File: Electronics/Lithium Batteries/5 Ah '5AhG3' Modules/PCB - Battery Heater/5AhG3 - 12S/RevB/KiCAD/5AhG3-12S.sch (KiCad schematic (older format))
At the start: 129 parts, among them J1 Screw_Terminal_01x02, J2 Screw_Terminal_01x02, J3 Screw_Terminal_01x03, J4 Screw_Terminal_01x03, J5 Conn_01x02, Q1 Q_NMOS_GDS, U1 APV1121S

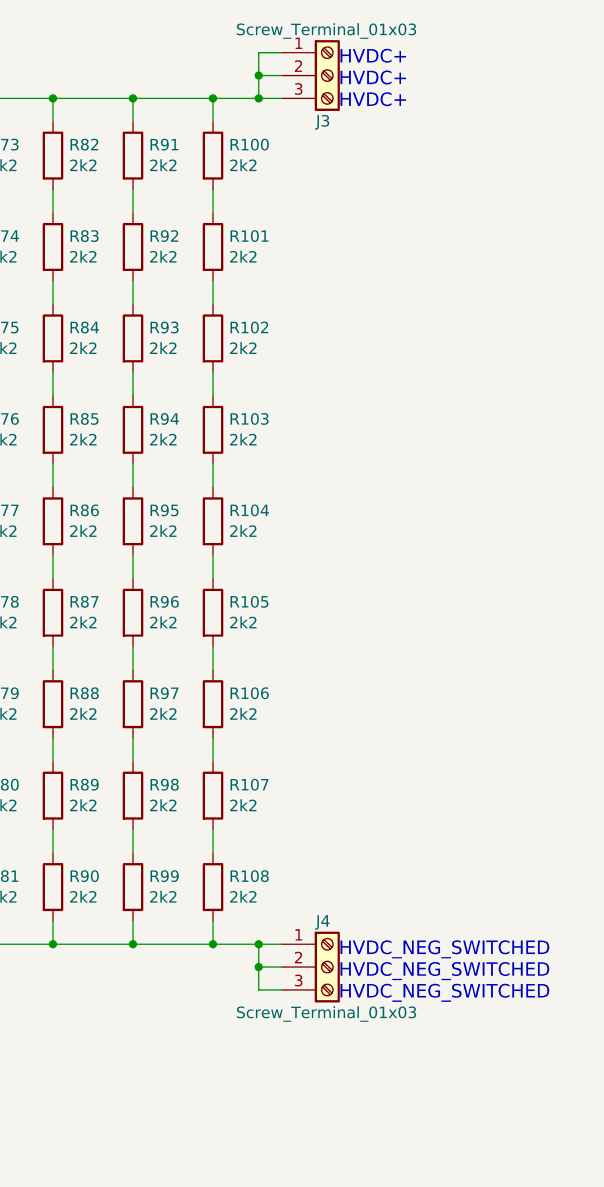
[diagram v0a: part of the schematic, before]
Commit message: RevB Heater PCBs, Daughterboard Schematic
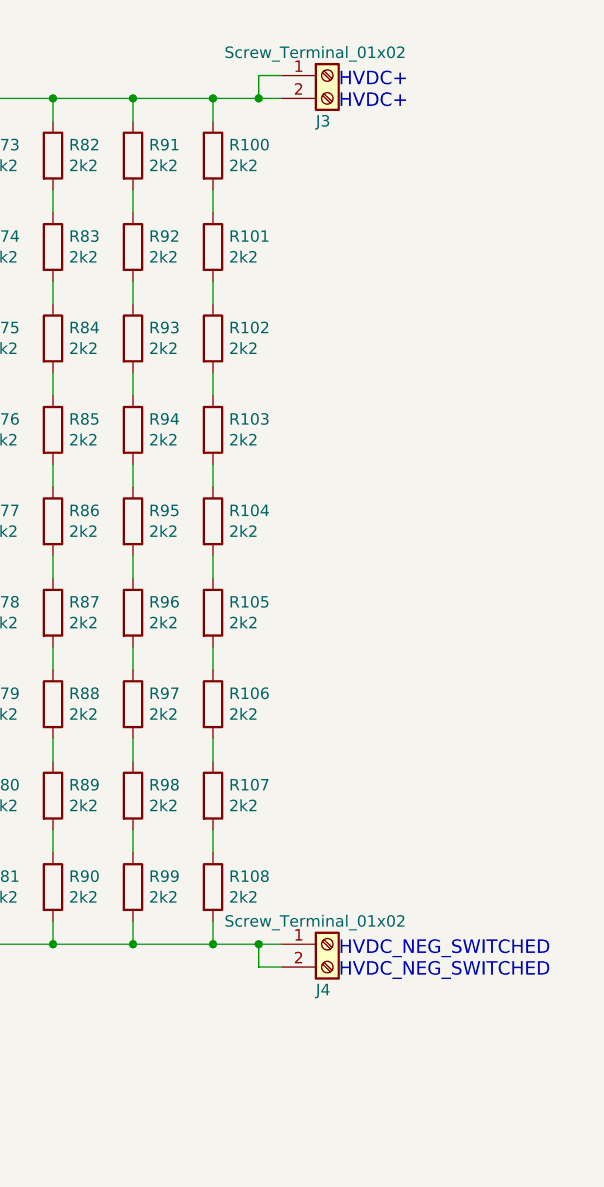
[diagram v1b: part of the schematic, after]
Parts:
- removed J3, J4: Screw_Terminal_01x03, Connector_Phoenix_MC:PhoenixContact_MCV_1,5_3-G-3.5_1x03_P3.50mm_Vertical, symbol Connector:Screw_Terminal_01x03
- added J3, J4: Screw_Terminal_01x02, Connector_Phoenix_MC:PhoenixContact_MCV_1,5_2-G-3.5_1x02_P3.50mm_Vertical, symbol Connector:Screw_Terminal_01x02
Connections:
- net HVDC_NEG_SWITCHED: now also J4.1 (Pin_1), J4.2 (Pin_2)
- net HVDC_POS: now also J3.1 (Pin_1), J3.2 (Pin_2)
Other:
- note added: "HVDC+\nHVDC+"
- note added: "HVDC_NEG_SWITCHED\nHVDC_NEG_SWITCHED"
- note removed: "HVDC+\nHVDC+\nHVDC+"
- note removed: "HVDC_NEG_SWITCHED\nHVDC_NEG_SWITCHED\nHVDC_NEG_SWITCHED"
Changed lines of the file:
@@
 Text Notes 4700 6050 0    50   ~ 0
 IPD70R360P7SAUMA1
-$Comp
-L Connector:Screw_Terminal_01x03 J3
-U 1 1 63B2CCAD
-P 10200 1650
-F 0 "J3" H 10150 1450 50  0000 L CNN
-F 1 "Screw_Terminal_01x03" H 9800 1850 50  0000 L CNN
-F 2 "Connector_Phoenix_MC:PhoenixContact_MCV_1,5_3-G-3.5_1x03_P3.50mm_Vertical" H 10200 1650 50  0001 C CNN
-F 3 "~" H 10200 1650 50  0001 C CNN
-	1    10200 1650
-	1    0    0    -1
-$EndComp
-$Comp
-L Connector:Screw_Terminal_01x03 J4
-U 1 1 63B2E862
-P 10200 5550
-F 0 "J4" H 10150 5750 50  0000 L CNN
-F 1 "Screw_Terminal_01x03" H 9800 5350 50  0000 L CNN
-F 2 "Connector_Phoenix_MC:PhoenixContact_MCV_1,5_3-G-3.5_1x03_P3.50mm_Vertical" H 10200 5550 50  0001 C CNN
-F 3 "~" H 10200 5550 50  0001 C CNN
-	1    10200 5550
-	1    0    0    -1
-$EndComp
 Wire Wire Line
 	9700 5450 9900 5450
-Wire Wire Line
-	10000 5650 9900 5650
-Wire Wire Line
-	9900 5650 9900 5550
 Connection ~ 9900 5450
 Wire Wire Line
@@
 Wire Wire Line
 	10000 5550 9900 5550
-Connection ~ 9900 5550
 Wire Wire Line
 	9900 5550 9900 5450
@@
 Wire Wire Line
 	9900 1750 9900 1650
-Wire Wire Line
-	9900 1550 10000 1550
 Connection ~ 9900 1750
 Wire Wire Line
@@
 Wire Wire Line
 	10000 1650 9900 1650
-Connection ~ 9900 1650
-Wire Wire Line
-	9900 1650 9900 1550
 Wire Wire Line
 	3300 6050 2650 6050
@@
 HVDC_POS_UNFUSED
 Text Notes 10250 1800 0    59   ~ 0
-HVDC+\nHVDC+\nHVDC+
+HVDC+\nHVDC+
 $Comp
 L Connector:Screw_Terminal_01x02 J2
@@
 	-1   0    0    1
 $EndComp
-Text Notes 10250 5700 0    59   ~ 0
-HVDC_NEG_SWITCHED\nHVDC_NEG_SWITCHED\nHVDC_NEG_SWITCHED
+Text Notes 10250 5600 0    59   ~ 0
+HVDC_NEG_SWITCHED\nHVDC_NEG_SWITCHED
 Wire Wire Line
 	5850 3350 5850 3600
@@
 	-1   0    0    1
 $EndComp
+$Comp
+L Connector:Screw_Terminal_01x02 J3
+U 1 1 63935938
+P 10200 1650
+F 0 "J3" H 10150 1450 50  0000 L CNN
+F 1 "Screw_Terminal_01x02" H 9750 1750 50  0000 L CNN
+F 2 "Connector_Phoenix_MC:PhoenixContact_MCV_1,5_2-G-3.5_1x02_P3.50mm_Vertical" H 10200 1650 50  0001 C CNN
+F 3 "~" H 10200 1650 50  0001 C CNN
+	1    10200 1650
+	1    0    0    -1
+$EndComp
+$Comp
+L Connector:Screw_Terminal_01x02 J4
+U 1 1 63943E3B
+P 10200 5450
+F 0 "J4" H 10150 5250 50  0000 L CNN
+F 1 "Screw_Terminal_01x02" H 9750 5550 50  0000 L CNN
+F 2 "Connector_Phoenix_MC:PhoenixContact_MCV_1,5_2-G-3.5_1x02_P3.50mm_Vertical" H 10200 5450 50  0001 C CNN
+F 3 "~" H 10200 5450 50  0001 C CNN
+	1    10200 5450
+	1    0    0    -1
+$EndComp
 $EndSCHEMATC
